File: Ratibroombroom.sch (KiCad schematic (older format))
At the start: 114 parts, among them J1 Conn_01x02_Male, J10 Conn_01x04_Male, J11 Conn_01x04_Male, J2 Conn_01x02_Male, J3 Conn_01x04_Male, J4 Conn_01x04_Male, J5 Conn_01x02_Male, J6 Conn_01x02_Male, J7 Conn_01x04_Male, J8 Conn_01x04_Male, J9 Conn_01x04_Male, Q1 IRLML6344, Q10 S8050, Q11 IRF7416PbF, Q2 IRLML6344, Q3 IRLML6344, Q4 IRLML6344, Q5 PT12-21B/TR8, Q6 PT12-21B/TR8, Q7 PT12-21B/TR8, Q8 PT12-21B/TR8, Q9 IRLML6344, SW1 B3U, SW2 B3U, SW3 PCM12, U1 AZ1117-3.3, U2 DRV8835, U3 AS5145B-HSST, U4 MPU-9250, U5 STM32F405RGTx, U6 AS5145B-HSST, U7 DRV8835, U8 L6932D1.2TR, U9 L6932D1.2TR, Y1 8MHZ

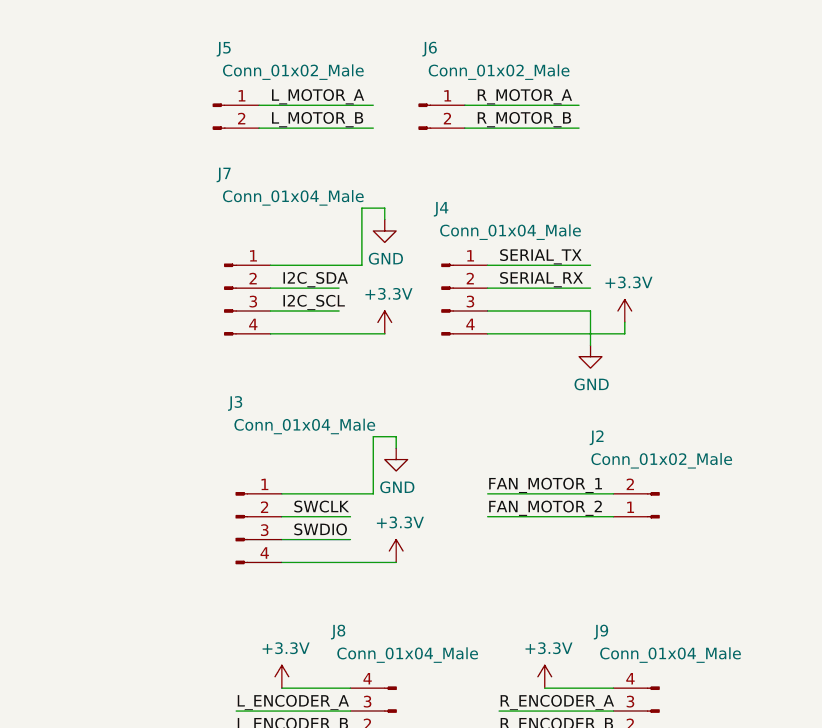
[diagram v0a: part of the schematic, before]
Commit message: Modify board to 45mm width to make everything fit. Place components in pcbnew Modify schematic to merge I2C, SWIO and UART connectors into a single 2x5 pin connector
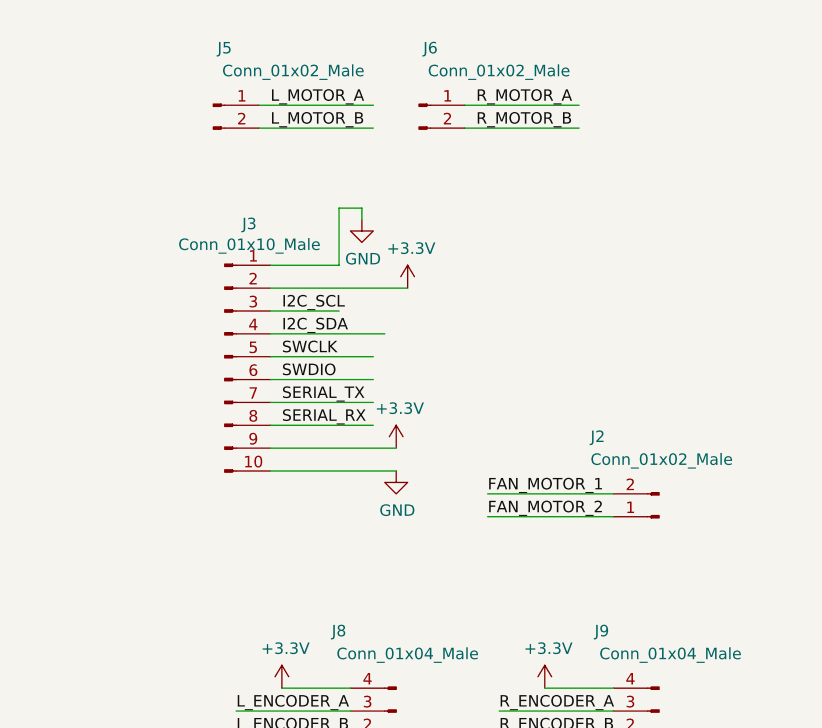
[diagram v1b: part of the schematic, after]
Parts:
- removed J3, J4, J7: Conn_01x04_Male, Connector_PinHeader_2.54mm:PinHeader_1x04_P2.54mm_Vertical, symbol Connector:Conn_01x04_Male
- added J3: Conn_01x10_Male, Connector_PinHeader_1.27mm:PinHeader_2x05_P1.27mm_Vertical, symbol Connector:Conn_01x10_Male
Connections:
- wire segments 424 -> 417
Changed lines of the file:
@@
 Text Label 3450 9550 0    50   ~ 0
 BUZZER
-$Comp
-L Connector:Conn_01x04_Male J3
-U 1 1 5ECADD95
-P 7600 7250
-F 0 "J3" H 7600 7750 50  0000 C CNN
-F 1 "Conn_01x04_Male" H 7900 7650 50  0000 C CNN
-F 2 "Connector_PinHeader_2.54mm:PinHeader_1x04_P2.54mm_Vertical" H 7600 7250 50  0001 C CNN
-F 3 "~" H 7600 7250 50  0001 C CNN
-	1    7600 7250
-	1    0    0    -1
-$EndComp
-$Comp
-L power:GND #PWR0103
-U 1 1 5ECC4EED
+Text Label 7800 6550 0    50   ~ 0
+SWCLK
+Text Label 7800 6650 0    50   ~ 0
+SWDIO
+Text Label 7800 6750 0    50   ~ 0
+SERIAL_TX
+Text Label 7800 6850 0    50   ~ 0
+SERIAL_RX
+$Comp
+L power:+3.3V #PWR0105
+U 1 1 5EDC1036
 P 8300 6950
-F 0 "#PWR0103" H 8300 6700 50  0001 C CNN
-F 1 "GND" H 8305 6777 50  0000 C CNN
+F 0 "#PWR0105" H 8300 6800 50  0001 C CNN
+F 1 "+3.3V" H 8315 7123 50  0000 C CNN
 F 2 "" H 8300 6950 50  0001 C CNN
 F 3 "" H 8300 6950 50  0001 C CNN
@@
 	1    0    0    -1
 $EndComp
-Text Label 7850 7250 0    50   ~ 0
-SWCLK
-Text Label 7850 7350 0    50   ~ 0
-SWDIO
-Wire Wire Line
-	8300 6900 8300 6950
-Wire Wire Line
-	7800 7250 8100 7250
-Wire Wire Line
-	7800 7350 8100 7350
-$Comp
-L power:+3.3V #PWR0104
-U 1 1 5ED8F83D
-P 8300 7450
-F 0 "#PWR0104" H 8300 7300 50  0001 C CNN
-F 1 "+3.3V" H 8315 7623 50  0000 C CNN
-F 2 "" H 8300 7450 50  0001 C CNN
-F 3 "" H 8300 7450 50  0001 C CNN
-	1    8300 7450
-	1    0    0    -1
-$EndComp
-Wire Wire Line
-	7800 7450 8300 7450
-$Comp
-L Connector:Conn_01x04_Male J4
-U 1 1 5EDBF6A6
-P 8500 6250
-F 0 "J4" H 8500 6600 50  0000 C CNN
-F 1 "Conn_01x04_Male" H 8800 6500 50  0000 C CNN
-F 2 "Connector_PinHeader_2.54mm:PinHeader_1x04_P2.54mm_Vertical" H 8500 6250 50  0001 C CNN
-F 3 "~" H 8500 6250 50  0001 C CNN
-	1    8500 6250
-	1    0    0    -1
-$EndComp
-Text Label 8750 6150 0    50   ~ 0
-SERIAL_TX
-Text Label 8750 6250 0    50   ~ 0
-SERIAL_RX
-$Comp
-L power:+3.3V #PWR0105
-U 1 1 5EDC1036
-P 9300 6400
-F 0 "#PWR0105" H 9300 6250 50  0001 C CNN
-F 1 "+3.3V" H 9315 6573 50  0000 C CNN
-F 2 "" H 9300 6400 50  0001 C CNN
-F 3 "" H 9300 6400 50  0001 C CNN
-	1    9300 6400
-	1    0    0    -1
-$EndComp
 $Comp
 L power:GND #PWR0106
 U 1 1 5EDC1658
-P 9150 6500
-F 0 "#PWR0106" H 9150 6250 50  0001 C CNN
-F 1 "GND" H 9155 6327 50  0000 C CNN
-F 2 "" H 9150 6500 50  0001 C CNN
-F 3 "" H 9150 6500 50  0001 C CNN
-	1    9150 6500
-	1    0    0    -1
-$EndComp
-Wire Wire Line
-	8700 6350 9150 6350
-Wire Wire Line
-	9150 6350 9150 6500
-Wire Wire Line
-	8700 6450 9300 6450
-Wire Wire Line
-	9300 6450 9300 6400
-Wire Wire Line
-	8700 6250 9150 6250
-Wire Wire Line
-	8700 6150 9150 6150
+P 8300 7050
+F 0 "#PWR0106" H 8300 6800 50  0001 C CNN
+F 1 "GND" H 8305 6877 50  0000 C CNN
+F 2 "" H 8300 7050 50  0001 C CNN
+F 3 "" H 8300 7050 50  0001 C CNN
+	1    8300 7050
+	1    0    0    -1
+$EndComp
+Wire Wire Line
+	7750 6650 8200 6650
+Wire Wire Line
+	7750 6550 8200 6550
 $Comp
 L Connector:Conn_01x02_Male J5
@@
 	13000 4250 13000 4300
 $Comp
-L Connector:Conn_01x04_Male J7
-U 1 1 5F36C05A
-P 7550 6250
-F 0 "J7" H 7550 6750 50  0000 C CNN
-F 1 "Conn_01x04_Male" H 7850 6650 50  0000 C CNN
-F 2 "Connector_PinHeader_2.54mm:PinHeader_1x04_P2.54mm_Vertical" H 7550 6250 50  0001 C CNN
-F 3 "~" H 7550 6250 50  0001 C CNN
-	1    7550 6250
-	1    0    0    -1
-$EndComp
-$Comp
 L power:GND #PWR0107
 U 1 1 5F36C066
-P 8250 5950
-F 0 "#PWR0107" H 8250 5700 50  0001 C CNN
-F 1 "GND" H 8255 5777 50  0000 C CNN
-F 2 "" H 8250 5950 50  0001 C CNN
-F 3 "" H 8250 5950 50  0001 C CNN
-	1    8250 5950
-	1    0    0    -1
-$EndComp
-Text Label 7800 6250 0    50   ~ 0
+P 8150 5950
+F 0 "#PWR0107" H 8150 5700 50  0001 C CNN
+F 1 "GND" H 8155 5777 50  0000 C CNN
+F 2 "" H 8150 5950 50  0001 C CNN
+F 3 "" H 8150 5950 50  0001 C CNN
+	1    8150 5950
+	1    0    0    -1
+$EndComp
+Text Label 7800 6450 0    50   ~ 0
 I2C_SDA
 Text Label 7800 6350 0    50   ~ 0
 I2C_SCL
 Wire Wire Line
-	8250 5900 8250 5950
-Wire Wire Line
-	7750 6250 8050 6250
+	8150 5900 8150 5950
 Wire Wire Line
 	7750 6350 8050 6350
@@
 L power:+3.3V #PWR0108
 U 1 1 5F36C075
-P 8250 6450
-F 0 "#PWR0108" H 8250 6300 50  0001 C CNN
-F 1 "+3.3V" H 8265 6623 50  0000 C CNN
-F 2 "" H 8250 6450 50  0001 C CNN
-F 3 "" H 8250 6450 50  0001 C CNN
-	1    8250 6450
+P 8350 6250
+F 0 "#PWR0108" H 8350 6100 50  0001 C CNN
+F 1 "+3.3V" H 8365 6423 50  0000 C CNN
+F 2 "" H 8350 6250 50  0001 C CNN
+F 3 "" H 8350 6250 50  0001 C CNN
+	1    8350 6250
 	1    0    0    -1
 $EndComp
@@
 Microcontroller
 Wire Wire Line
-	7800 7150 8200 7150
-Wire Wire Line
-	8200 7150 8200 6900
-Wire Wire Line
-	8200 6900 8300 6900
-Wire Wire Line
-	7750 6150 8150 6150
-Wire Wire Line
-	8150 6150 8150 5900
-Wire Wire Line
-	8150 5900 8250 5900
+	7750 6150 8050 6150
+Wire Wire Line
+	8050 6150 8050 5900
+Wire Wire Line
+	8050 5900 8150 5900
 Text Notes 7700 5000 0    118  ~ 24
 Connectors
@@
 Text Notes 6900 2650 0    50   ~ 0
 Calcular valores das resistencias\nde emisores e receptores
+$Comp
+L Connector:Conn_01x10_Male J3
+U 1 1 5E6DC64F
+P 7550 6550
+F 0 "J3" H 7658 7131 50  0000 C CNN
+F 1 "Conn_01x10_Male" H 7658 7040 50  0000 C CNN
+F 2 "Connector_PinHeader_1.27mm:PinHeader_2x05_P1.27mm_Vertical" H 7550 6550 50  0001 C CNN
+F 3 "~" H 7550 6550 50  0001 C CNN
+	1    7550 6550
+	1    0    0    -1
+$EndComp
+Wire Wire Line
+	7750 6750 8200 6750
+Wire Wire Line
+	7750 7050 8300 7050
+Wire Wire Line
+	7750 6950 8300 6950
+Wire Wire Line
+	7750 6850 8200 6850
+Wire Wire Line
+	7750 6250 8350 6250
 $EndSCHEMATC

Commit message: Change encoder board connector footprint to single side connector
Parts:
- J10, J11: footprint Ratibroombroom:Edge_connector_4P_1x3mm -> Ratibroombroom:Pad_SMD_4P_1x3mm
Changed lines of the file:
@@
 F 0 "J10" H 13850 8300 50  0000 C CNN
 F 1 "Conn_01x04_Male" V 13550 8750 50  0000 C CNN
-F 2 "Ratibroombroom:Edge_connector_4P_1x3mm" H 13600 8750 50  0001 C CNN
+F 2 "Ratibroombroom:Pad_SMD_4P_1x3mm" H 13600 8750 50  0001 C CNN
 F 3 "~" H 13600 8750 50  0001 C CNN
 	1    13600 8750
@@
 F 0 "J11" H 16100 8300 50  0000 C CNN
 F 1 "Conn_01x04_Male" V 15800 8750 50  0000 C CNN
-F 2 "Ratibroombroom:Edge_connector_4P_1x3mm" H 15850 8750 50  0001 C CNN
+F 2 "Ratibroombroom:Pad_SMD_4P_1x3mm" H 15850 8750 50  0001 C CNN
 F 3 "~" H 15850 8750 50  0001 C CNN
 	1    15850 8750

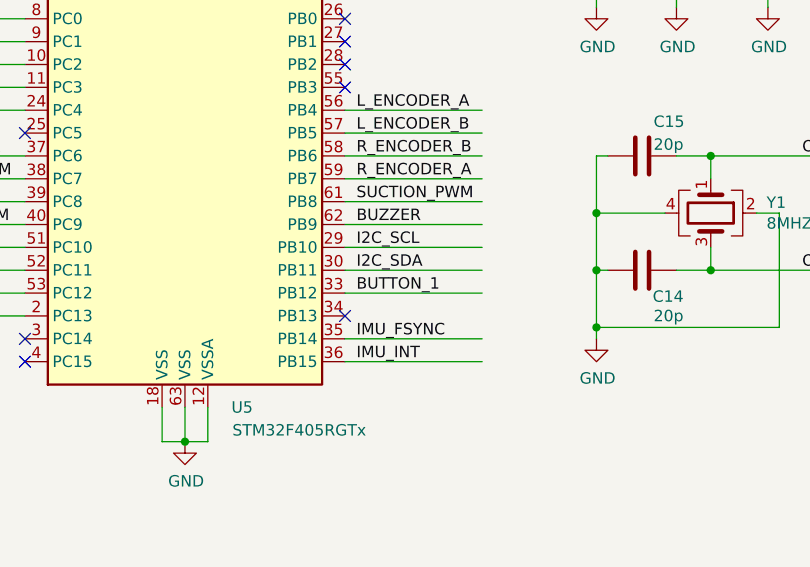
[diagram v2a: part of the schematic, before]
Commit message: Partial PCB routing
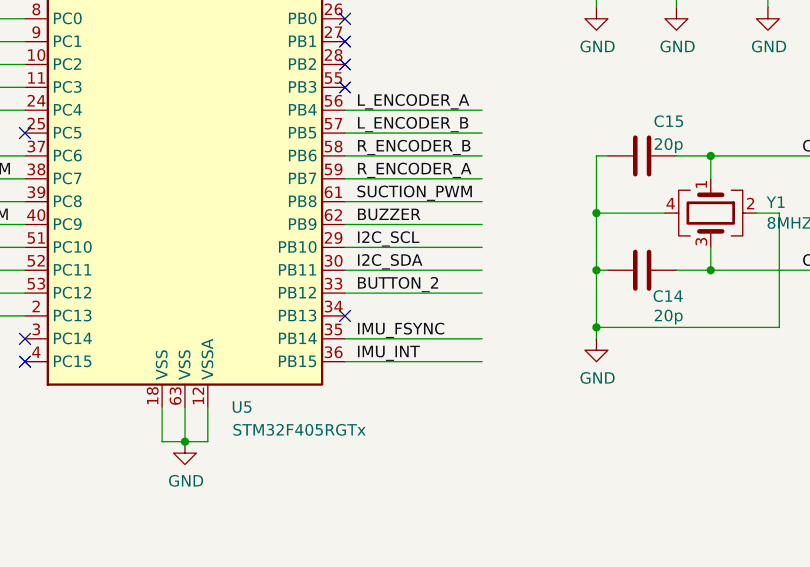
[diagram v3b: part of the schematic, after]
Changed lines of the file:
@@
 EESchema Schematic File Version 4
-LIBS:Ratibroombroom-cache
-EELAYER 29 0
+EELAYER 30 0
 EELAYER END
 $Descr A3 16535 11693
@@
 NoConn ~ 2000 10050
 Text Label 3450 9850 0    50   ~ 0
-BUTTON_1
+BUTTON_2
 Wire Wire Line
 	3400 9850 4000 9850
